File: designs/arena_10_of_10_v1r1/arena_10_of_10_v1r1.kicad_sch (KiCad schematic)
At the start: 0 parts

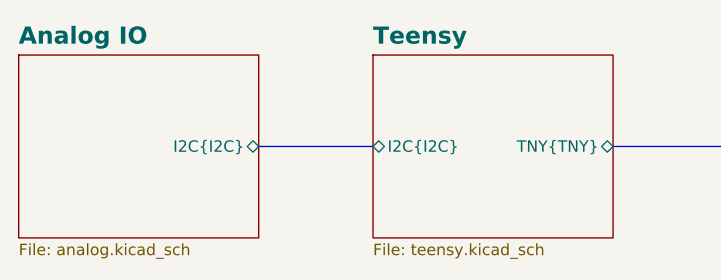
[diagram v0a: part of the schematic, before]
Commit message: Re-worked MISO handling and analog input circuit.
Modified so that MISO isolation circuits are in fan out section and
are such that they will be placed close to the teensy.  Modified the
analog input circuit so that the teensy MCU analog inputs are used in
conjuction with a level shifting circuit.
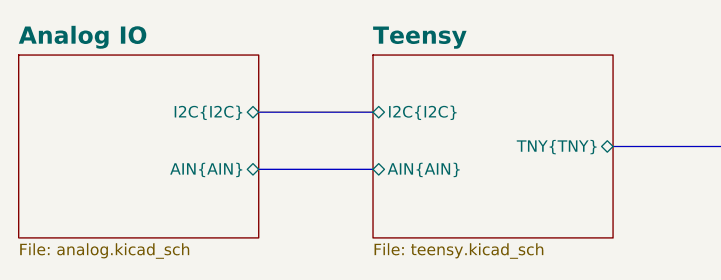
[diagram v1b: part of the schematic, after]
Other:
- sheet Analog IO ports: added AIN{AIN}; removed none
- sheet Teensy ports: added AIN{AIN}; removed none
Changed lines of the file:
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@@
 	(generator_version "9.0")
 	(paper "A4")
+	(bus_alias "AIN"
+		(members "A0" "A1")
+	)
 	(bus_alias "TNY"
 		(members "SCK_B0" "MOSI_B0" "MISO_B0" "SCK_B1" "MOSI_B1" "MISO_B1" "CS_00"
@@
 	(bus
 		(pts
-			(xy 101.6 45.72) (xy 114.3 45.72)
+			(xy 62.23 41.91) (xy 74.93 41.91)
 		)
 		(stroke
@@
 	(bus
 		(pts
-			(xy 62.23 45.72) (xy 74.93 45.72)
+			(xy 101.6 45.72) (xy 114.3 45.72)
+		)
+		(stroke
+			(width 0)
+			(type default)
+		)
+	)
+	(bus
+		(pts
+			(xy 62.23 48.26) (xy 74.93 48.26)
 		)
 		(stroke
@@
 		)
 		(pin "I2C{I2C}" bidirectional
-			(at 74.93 45.72 180)
+			(at 74.93 41.91 180)
 			(effects
 				(font
@@
 				)
 				(justify right)
+			)
+		)
+		(pin "AIN{AIN}" bidirectional
+			(at 74.93 48.26 180)
+			(effects
+				(font
+					(size 1.27 1.27)
+				)
+				(justify left)
 			)
 		)
@@
 		)
 		(pin "I2C{I2C}" bidirectional
-			(at 62.23 45.72 0)
-			(effects
-				(font
+			(at 62.23 41.91 0)
+			(effects
+				(font
+					(size 1.27 1.27)
+				)
+				(justify right)
+			)
+		)
+		(pin "AIN{AIN}" bidirectional
+			(at 62.23 48.26 0)
+			(effects
+				(font
